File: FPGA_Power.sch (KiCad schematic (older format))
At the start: 79 parts, among them U1 XA7Z020-1CLG400Q

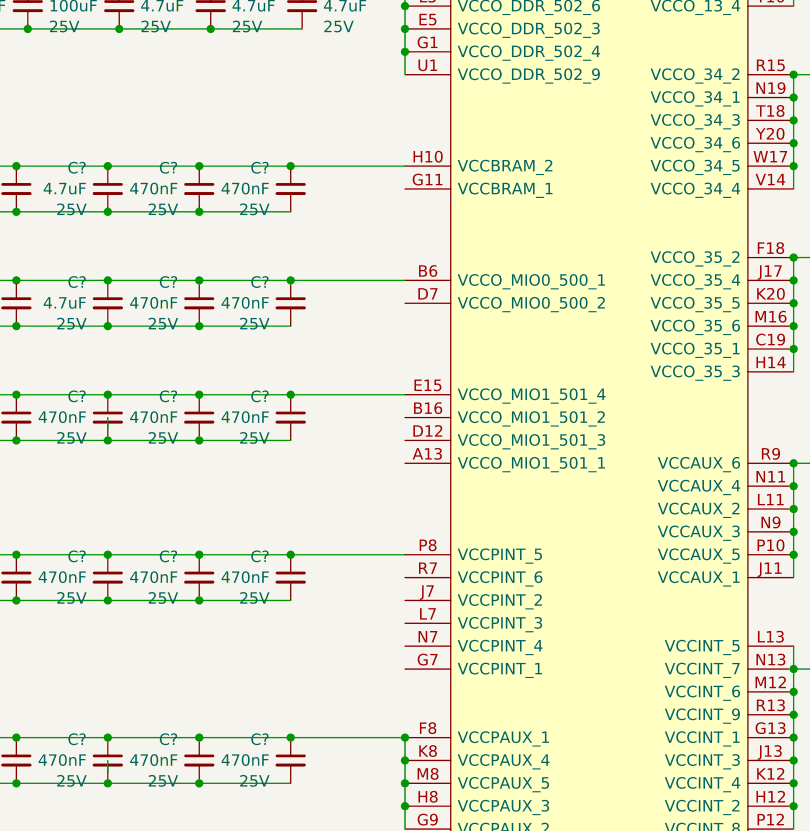
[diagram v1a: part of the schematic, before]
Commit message: Added nets for fx3 usb3 cct from fpga
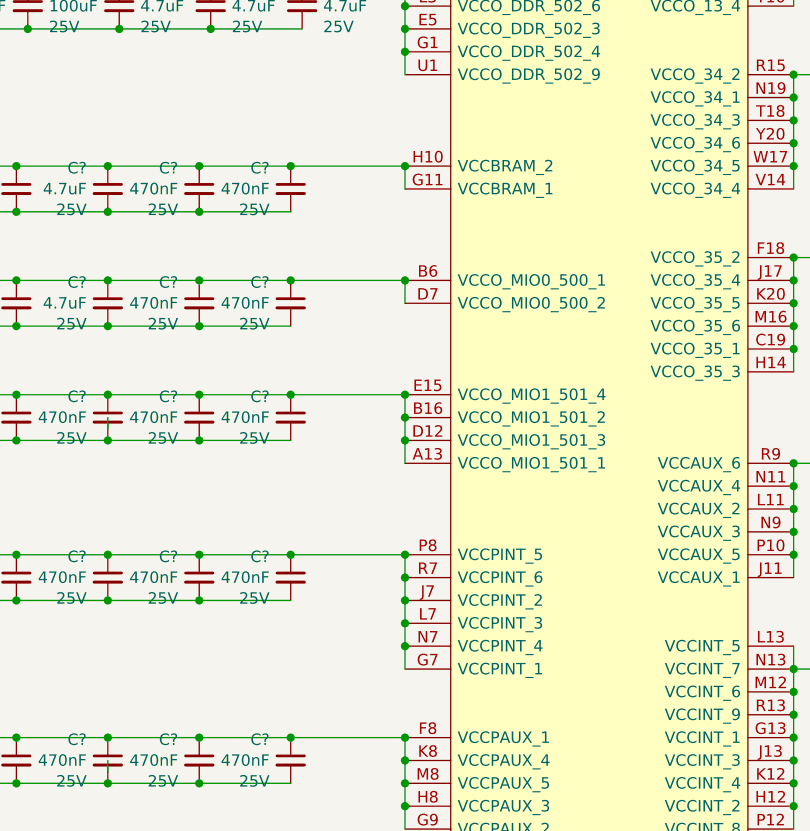
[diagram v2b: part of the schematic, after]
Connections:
- wire segments 270 -> 280
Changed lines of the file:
@@
 	1    0    0    -1
 $EndComp
+Wire Wire Line
+	5500 4150 5500 4050
+Connection ~ 5500 4050
+Connection ~ 5500 4550
+Wire Wire Line
+	5500 5350 5500 5250
+Connection ~ 5500 5050
+Connection ~ 5500 5150
+Wire Wire Line
+	5500 5150 5500 5050
+Connection ~ 5500 5250
+Wire Wire Line
+	5500 5250 5500 5150
+Connection ~ 5500 5750
+Connection ~ 5500 5850
+Wire Wire Line
+	5500 5850 5500 5750
+Connection ~ 5500 5950
+Wire Wire Line
+	5500 5950 5500 5850
+Connection ~ 5500 6050
+Wire Wire Line
+	5500 6050 5500 5950
+Wire Wire Line
+	5500 6050 5500 6150
+Connection ~ 5500 6150
+Wire Wire Line
+	5500 6150 5500 6250
+Wire Wire Line
+	5500 4550 5500 4650
 $EndSCHEMATC

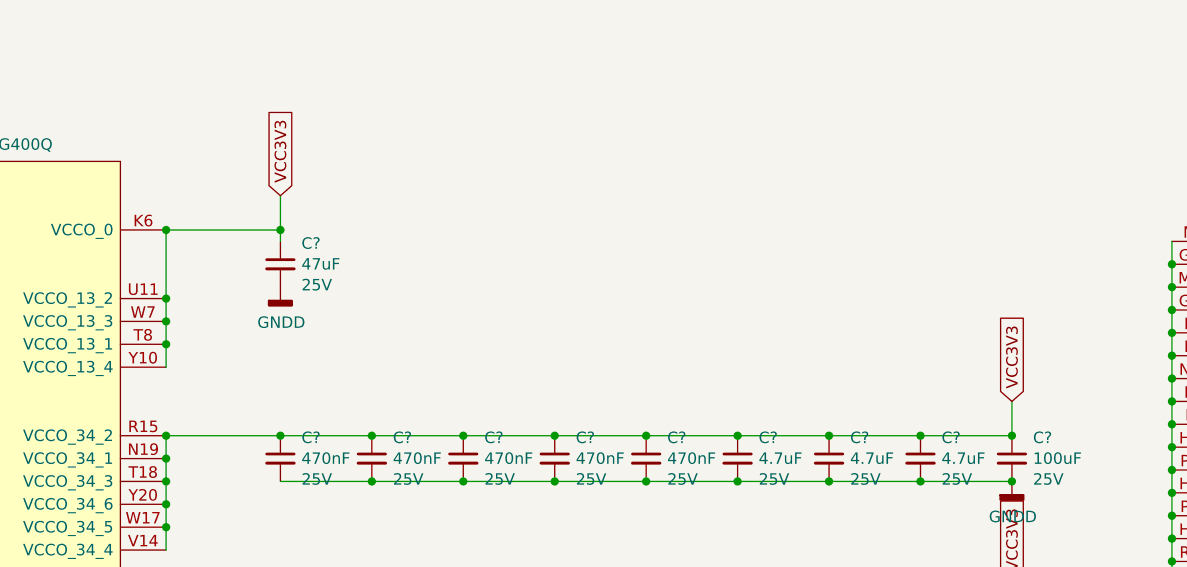
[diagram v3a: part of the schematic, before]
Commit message: Changed Bank13 deoupling caps and set the bank voltage to 2.5V
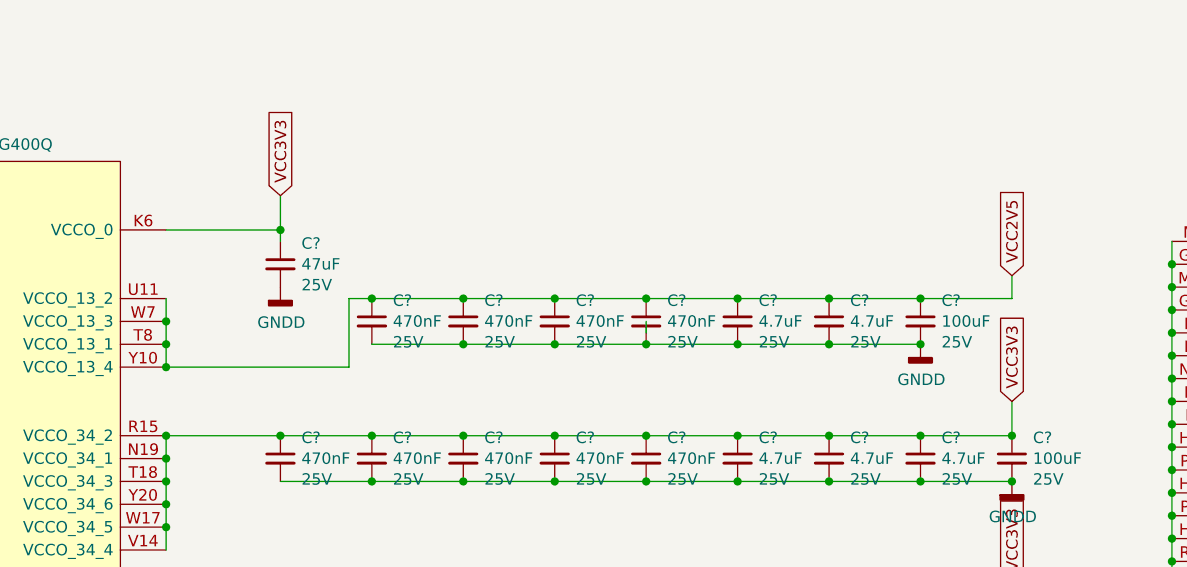
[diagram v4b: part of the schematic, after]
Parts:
- added C? (x4): 470nF, Capacitor_SMD:C_0603_1608Metric_Pad1.08x0.95mm_HandSolder, symbol Device:C_Small
- added C? (x2): 4.7uF, Capacitor_SMD:C_0603_1608Metric_Pad1.08x0.95mm_HandSolder, symbol Device:C_Small
- added C?: 100uF, Capacitor_SMD:C_1210_3225Metric_Pad1.33x2.70mm_HandSolder, symbol Device:C_Small
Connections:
- net labels added: VCC2V5
- wire segments 280 -> 297
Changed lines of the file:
@@
 	1    0    0    -1
 $EndComp
-Text GLabel 7700 2600 1    50   Input ~ 0
-VCC3V3
 Wire Wire Line
 	7200 2750 7700 2750
@@
 Wire Wire Line
 	7200 3350 7200 3250
-Connection ~ 7200 2750
-Connection ~ 7200 3050
-Wire Wire Line
-	7200 3050 7200 2750
 Connection ~ 7200 3150
 Wire Wire Line
@@
 Wire Wire Line
 	5500 4550 5500 4650
+Text GLabel 7700 2600 1    50   Input ~ 0
+VCC3V3
+$Comp
+L Device:C_Small C?
+U 1 1 604FF7B3
+P 8900 3150
+AR Path="/601E7C5A/604FF7B3" Ref="C?"  Part="1"
+AR Path="/601E7CC8/604FF7B3" Ref="C?"  Part="1"
+AR Path="/601E7C92/604FF7B3" Ref="C?"  Part="1"
+AR Path="/601E7C92/60257FE5/604FF7B3" Ref="C?"  Part="1"
+AR Path="/601E7B38/604FF7B3" Ref="C?"  Part="1"
+AR Path="/601DF0A6/604FF7B3" Ref="C?"  Part="1"
+AR Path="/601E7A84/604FF7B3" Ref="C?"  Part="1"
+F 0 "C?" H 8992 3241 50  0000 L CNN
+F 1 "470nF" H 8992 3150 50  0000 L CNN
+F 2 "Capacitor_SMD:C_0603_1608Metric_Pad1.08x0.95mm_HandSolder" H 8900 3150 50  0001 C CNN
+F 3 "~" H 8900 3150 50  0001 C CNN
+F 4 "25V" H 8992 3059 50  0000 L CNN "Voltage"
+	1    8900 3150
+	1    0    0    -1
+$EndComp
+$Comp
+L Device:C_Small C?
+U 1 1 604FF7BA
+P 9300 3150
+AR Path="/601E7C5A/604FF7BA" Ref="C?"  Part="1"
+AR Path="/601E7CC8/604FF7BA" Ref="C?"  Part="1"
+AR Path="/601E7C92/604FF7BA" Ref="C?"  Part="1"
+AR Path="/601E7C92/60257FE5/604FF7BA" Ref="C?"  Part="1"
+AR Path="/601E7B38/604FF7BA" Ref="C?"  Part="1"
+AR Path="/601DF0A6/604FF7BA" Ref="C?"  Part="1"
+AR Path="/601E7A84/604FF7BA" Ref="C?"  Part="1"
+F 0 "C?" H 9392 3241 50  0000 L CNN
+F 1 "470nF" H 9392 3150 50  0000 L CNN
+F 2 "Capacitor_SMD:C_0603_1608Metric_Pad1.08x0.95mm_HandSolder" H 9300 3150 50  0001 C CNN
+F 3 "~" H 9300 3150 50  0001 C CNN
+F 4 "25V" H 9392 3059 50  0000 L CNN "Voltage"
+	1    9300 3150
+	1    0    0    -1
+$EndComp
+Connection ~ 8900 3050
+Connection ~ 9300 3050
+Wire Wire Line
+	9300 3050 8900 3050
+Connection ~ 9300 3250
+Wire Wire Line
+	9300 3250 8900 3250
+$Comp
+L Device:C_Small C?
+U 1 1 604FF7C6
+P 9700 3150
+AR Path="/601E7C5A/604FF7C6" Ref="C?"  Part="1"
+AR Path="/601E7CC8/604FF7C6" Ref="C?"  Part="1"
+AR Path="/601E7C92/604FF7C6" Ref="C?"  Part="1"
+AR Path="/601E7C92/60257FE5/604FF7C6" Ref="C?"  Part="1"
+AR Path="/601E7B38/604FF7C6" Ref="C?"  Part="1"
+AR Path="/601DF0A6/604FF7C6" Ref="C?"  Part="1"
+AR Path="/601E7A84/604FF7C6" Ref="C?"  Part="1"
+F 0 "C?" H 9792 3241 50  0000 L CNN
+F 1 "4.7uF" H 9792 3150 50  0000 L CNN
+F 2 "Capacitor_SMD:C_0603_1608Metric_Pad1.08x0.95mm_HandSolder" H 9700 3150 50  0001 C CNN
+F 3 "~" H 9700 3150 50  0001 C CNN
+F 4 "25V" H 9792 3059 50  0000 L CNN "Voltage"
+	1    9700 3150
+	1    0    0    -1
+$EndComp
+$Comp
+L Device:C_Small C?
+U 1 1 604FF7CD
+P 10100 3150
+AR Path="/601E7C5A/604FF7CD" Ref="C?"  Part="1"
+AR Path="/601E7CC8/604FF7CD" Ref="C?"  Part="1"
+AR Path="/601E7C92/604FF7CD" Ref="C?"  Part="1"
+AR Path="/601E7C92/60257FE5/604FF7CD" Ref="C?"  Part="1"
+AR Path="/601E7B38/604FF7CD" Ref="C?"  Part="1"
+AR Path="/601DF0A6/604FF7CD" Ref="C?"  Part="1"
+AR Path="/601E7A84/604FF7CD" Ref="C?"  Part="1"
+F 0 "C?" H 10192 3241 50  0000 L CNN
+F 1 "4.7uF" H 10192 3150 50  0000 L CNN
+F 2 "Capacitor_SMD:C_0603_1608Metric_Pad1.08x0.95mm_HandSolder" H 10100 3150 50  0001 C CNN
+F 3 "~" H 10100 3150 50  0001 C CNN
+F 4 "25V" H 10192 3059 50  0000 L CNN "Voltage"
+	1    10100 3150
+	1    0    0    -1
+$EndComp
+Connection ~ 9700 3050
+Wire Wire Line
+	9700 3050 10100 3050
+Wire Wire Line
+	10500 3050 10900 3050
+Wire Wire Line
+	10500 3250 10100 3250
+Connection ~ 9700 3250
+Connection ~ 10100 3250
+Wire Wire Line
+	10100 3250 9700 3250
+Wire Wire Line
+	9300 3050 9700 3050
+Wire Wire Line
+	9300 3250 9700 3250
+$Comp
+L power:GNDD #PWR?
+U 1 1 604FF7DC
+P 10500 3250
+AR Path="/601DF0A6/604FF7DC" Ref="#PWR?"  Part="1"
+AR Path="/601E7C5A/604FF7DC" Ref="#PWR?"  Part="1"
+AR Path="/601E7CC8/604FF7DC" Ref="#PWR?"  Part="1"
+AR Path="/601E7C92/604FF7DC" Ref="#PWR?"  Part="1"
+AR Path="/601E7C92/60257FE5/604FF7DC" Ref="#PWR?"  Part="1"
+AR Path="/601E7B38/604FF7DC" Ref="#PWR?"  Part="1"
+AR Path="/601E7A84/604FF7DC" Ref="#PWR?"  Part="1"
+F 0 "#PWR?" H 10500 3000 50  0001 C CNN
+F 1 "GNDD" H 10504 3095 50  0000 C CNN
+F 2 "" H 10500 3250 50  0001 C CNN
+F 3 "" H 10500 3250 50  0001 C CNN
+	1    10500 3250
+	1    0    0    -1
+$EndComp
+Text GLabel 10900 2950 1    50   Input ~ 0
+VCC2V5
+Wire Wire Line
+	10900 3050 10900 2950
+$Comp
+L Device:C_Small C?
+U 1 1 604FF7E5
+P 8100 3150
+AR Path="/601E7C5A/604FF7E5" Ref="C?"  Part="1"
+AR Path="/601E7CC8/604FF7E5" Ref="C?"  Part="1"
+AR Path="/601E7C92/604FF7E5" Ref="C?"  Part="1"
+AR Path="/601E7C92/60257FE5/604FF7E5" Ref="C?"  Part="1"
+AR Path="/601E7B38/604FF7E5" Ref="C?"  Part="1"
+AR Path="/601DF0A6/604FF7E5" Ref="C?"  Part="1"
+AR Path="/601E7A84/604FF7E5" Ref="C?"  Part="1"
+F 0 "C?" H 8192 3241 50  0000 L CNN
+F 1 "470nF" H 8192 3150 50  0000 L CNN
+F 2 "Capacitor_SMD:C_0603_1608Metric_Pad1.08x0.95mm_HandSolder" H 8100 3150 50  0001 C CNN
+F 3 "~" H 8100 3150 50  0001 C CNN
+F 4 "25V" H 8192 3059 50  0000 L CNN "Voltage"
+	1    8100 3150
+	1    0    0    -1
+$EndComp
+Wire Wire Line
+	8500 3050 8900 3050
+Wire Wire Line
+	9300 3200 9300 3150
+Wire Wire Line
+	8900 3250 8500 3250
+Connection ~ 8900 3250
+$Comp
+L Device:C_Small C?
+U 1 1 604FF7F2
+P 10500 3150
+AR Path="/601E7C5A/604FF7F2" Ref="C?"  Part="1"
+AR Path="/601E7CC8/604FF7F2" Ref="C?"  Part="1"
+AR Path="/601E7C92/604FF7F2" Ref="C?"  Part="1"
+AR Path="/601E7C92/60257FE5/604FF7F2" Ref="C?"  Part="1"
+AR Path="/601E7B38/604FF7F2" Ref="C?"  Part="1"
+AR Path="/601DF0A6/604FF7F2" Ref="C?"  Part="1"
+AR Path="/601E7A84/604FF7F2" Ref="C?"  Part="1"
+F 0 "C?" H 10592 3241 50  0000 L CNN
+F 1 "100uF" H 10592 3150 50  0000 L CNN
+F 2 "Capacitor_SMD:C_1210_3225Metric_Pad1.33x2.70mm_HandSolder" H 10500 3150 50  0001 C CNN
+F 3 "~" H 10500 3150 50  0001 C CNN
+F 4 "25V" H 10592 3059 50  0000 L CNN "Voltage"
+	1    10500 3150
+	1    0    0    -1
+$EndComp
+Connection ~ 10500 3250
+Wire Wire Line
+	10100 3050 10500 3050
+Connection ~ 10100 3050
+Connection ~ 10500 3050
+Wire Wire Line
+	7200 3350 8000 3350
+Wire Wire Line
+	8000 3350 8000 3050
+Wire Wire Line
+	8000 3050 8100 3050
+Connection ~ 7200 3350
+$Comp
+L Device:C_Small C?
+U 1 1 6057A9AA
+P 8500 3150
+AR Path="/601E7C5A/6057A9AA" Ref="C?"  Part="1"
+AR Path="/601E7CC8/6057A9AA" Ref="C?"  Part="1"
+AR Path="/601E7C92/6057A9AA" Ref="C?"  Part="1"
+AR Path="/601E7C92/60257FE5/6057A9AA" Ref="C?"  Part="1"
+AR Path="/601E7B38/6057A9AA" Ref="C?"  Part="1"
+AR Path="/601DF0A6/6057A9AA" Ref="C?"  Part="1"
+AR Path="/601E7A84/6057A9AA" Ref="C?"  Part="1"
+F 0 "C?" H 8592 3241 50  0000 L CNN
+F 1 "470nF" H 8592 3150 50  0000 L CNN
+F 2 "Capacitor_SMD:C_0603_1608Metric_Pad1.08x0.95mm_HandSolder" H 8500 3150 50  0001 C CNN
+F 3 "~" H 8500 3150 50  0001 C CNN
+F 4 "25V" H 8592 3059 50  0000 L CNN "Voltage"
+	1    8500 3150
+	1    0    0    -1
+$EndComp
+Wire Wire Line
+	8100 3050 8500 3050
+Connection ~ 8100 3050
+Connection ~ 8500 3050
+Wire Wire Line
+	8500 3250 8100 3250
+Connection ~ 8500 3250
 $EndSCHEMATC

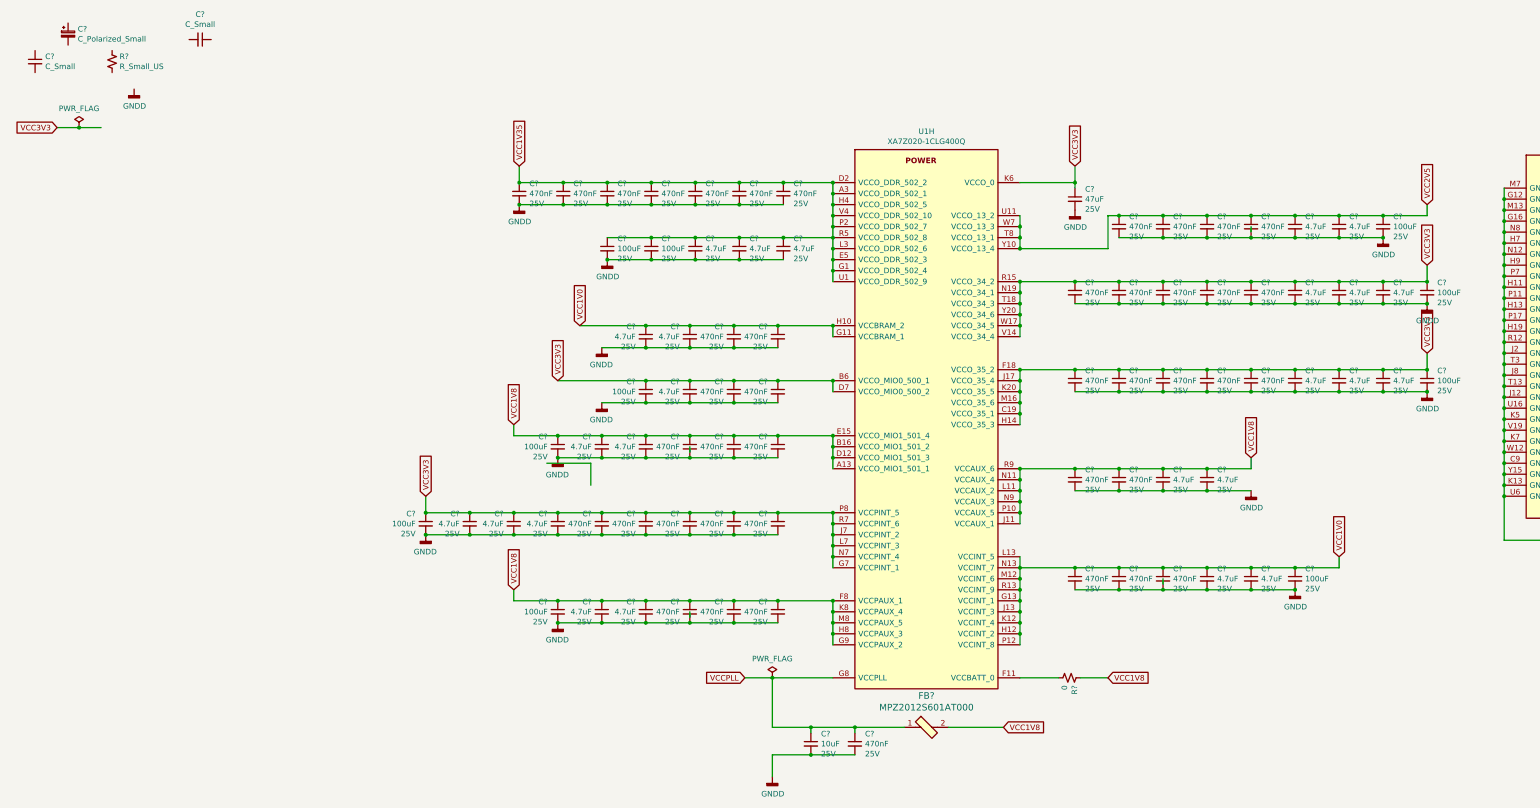
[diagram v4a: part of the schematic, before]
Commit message: PCB created and schematics annotated High speed connections added to the BTB
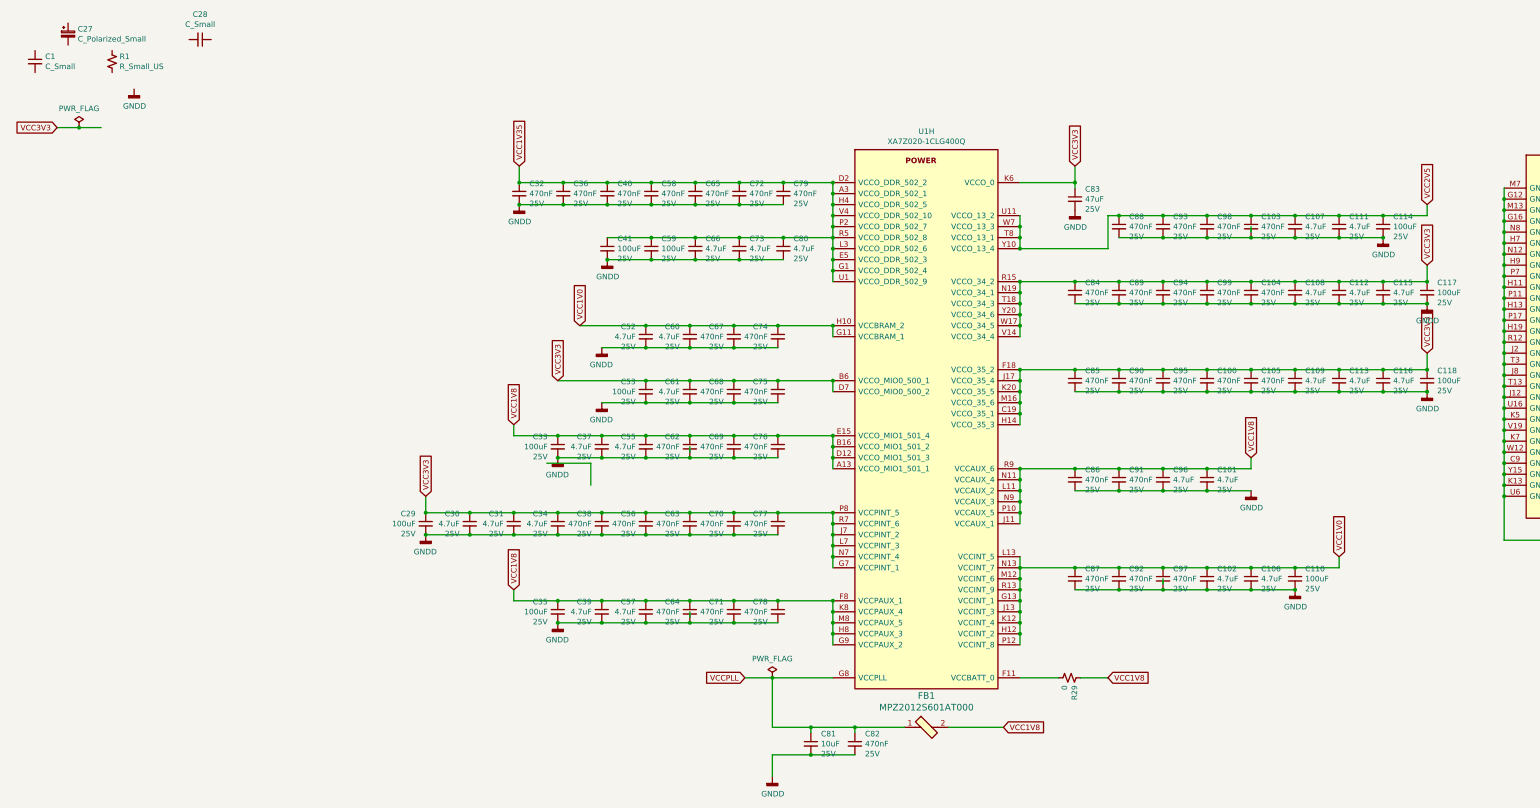
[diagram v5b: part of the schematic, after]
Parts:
- gave numbers to parts that had none: 85

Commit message: Corrected PCB import errors
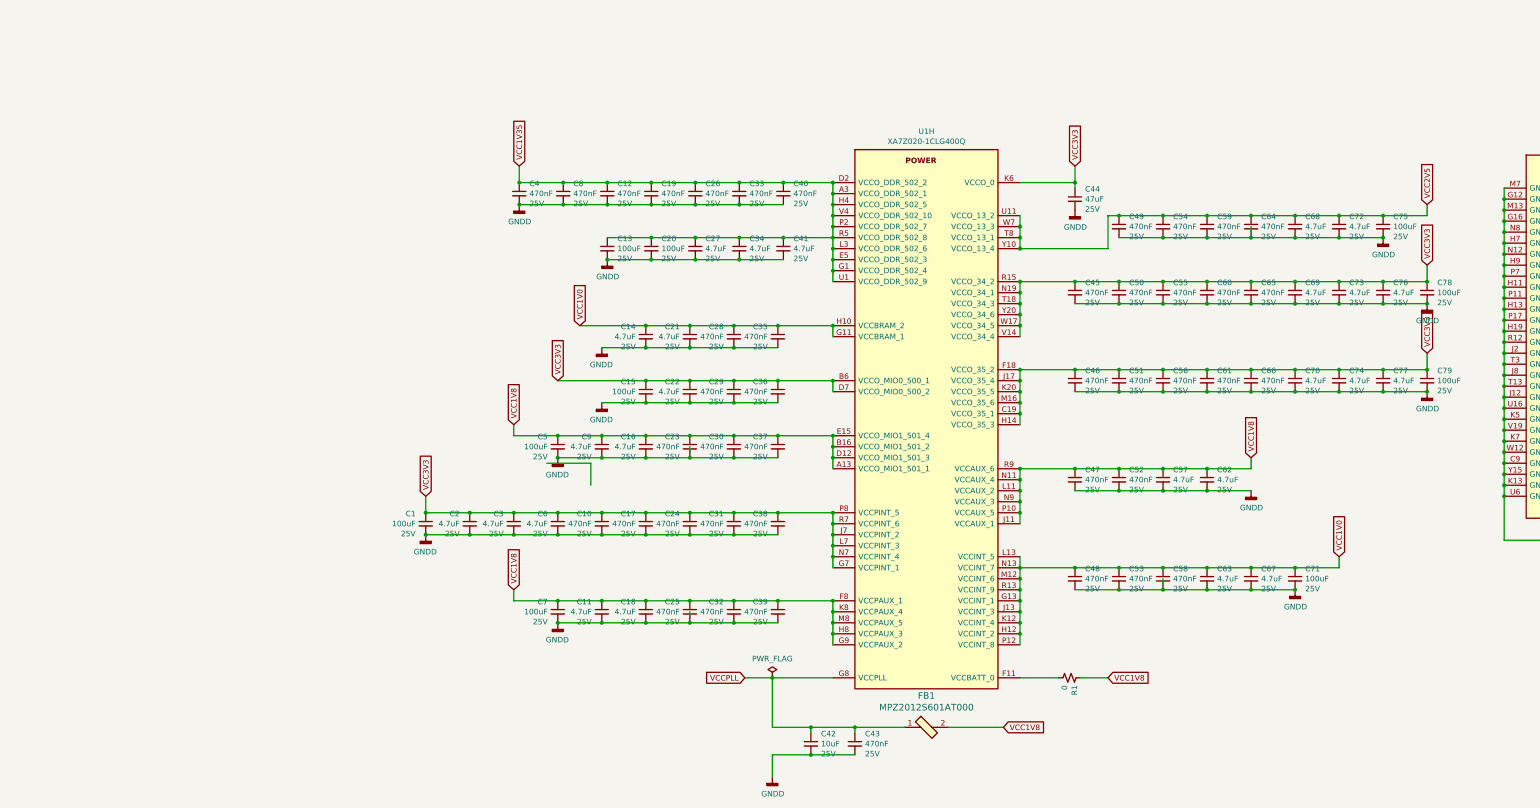
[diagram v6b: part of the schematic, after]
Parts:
- removed C1: C_Small, Capacitor_SMD:C_0603_1608Metric_Pad1.08x0.95mm_HandSolder, symbol Device:C_Small
- removed C27: C_Polarized_Small, Capacitor_Tantalum_SMD:CP_EIA-1608-10_AVX-L_Pad1.25x1.05mm_HandSolder, symbol Device:C_Polarized_Small
- removed C28: C_Small, symbol Device:C_Small
- removed R1: R_Small_US, Resistor_SMD:R_0603_1608Metric_Pad0.98x0.95mm_HandSolder, symbol Device:R_Small_US
- renumbered C29 to C1, C38 to C10, C39 to C11, C40 to C12, C41 to C13, C52 to C14, C53 to C15, C55 to C16, C56 to C17, C57 to C18, C58 to C19, C30 to C2, C59 to C20, C60 to C21, C61 to C22, C62 to C23, C63 to C24, C64 to C25, C65 to C26, C66 to C27, C67 to C28, C68 to C29, C31 to C3, C69 to C30, C70 to C31, C71 to C32, C72 to C33, C73 to C34, C74 to C35, C75 to C36, C76 to C37, C77 to C38, C78 to C39, C32 to C4, C79 to C40, C80 to C41, C81 to C42, C82 to C43, C83 to C44, C84 to C45, C85 to C46, C86 to C47, C87 to C48, C88 to C49, C33 to C5, C89 to C50, C90 to C51, C91 to C52, C92 to C53, C93 to C54, C94 to C55, C95 to C56, C96 to C57, C97 to C58, C98 to C59, C34 to C6, C99 to C60, C100 to C61, C101 to C62, C102 to C63, C103 to C64, C104 to C65, C105 to C66, C106 to C67, C107 to C68, C108 to C69, C35 to C7, C109 to C70, C110 to C71, C111 to C72, C112 to C73, C113 to C74, C114 to C75, C115 to C76, C116 to C77, C117 to C78, C118 to C79, C36 to C8, C37 to C9, R29 to R1
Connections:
- wire segments 297 -> 295
